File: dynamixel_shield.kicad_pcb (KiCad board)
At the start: 2 copper layers, 68.6 x 53.3 mm, 25 parts, among them P1 BARREL_JACK, P2 CONN_01X02, P3 CONN_01X03, P4 CONN_01X03, P5 CONN_01X03, P6 CONN_01X03, P7 CONN_01X03, P8 CONN_01X03, P9 CONN_01X03, Q1 MOSFET_N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

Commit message: Update silkscreen
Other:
- board text added: "10A MAX"
- board text added: "5A MAX"
- board text added: "POWER (12V)"
- board text added: "VIN POWER"
- board text removed: "VIN"
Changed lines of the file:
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@@
     (area 53.318999 50.945 132.842001 112.522001)
     (thickness 1.6)
-    (drawings 16)
+    (drawings 19)
     (tracks 185)
     (zones 0)
@@
     (visible_elements FFFFFF7F)
     (pcbplotparams
-      (layerselection 0x00030_80000001)
+      (layerselection 0x010f0_80000001)
       (usegerberextensions false)
       (excludeedgelayer true)
@@
       (outputformat 1)
       (mirror false)
-      (drillshape 1)
+      (drillshape 0)
       (scaleselection 1)
-      (outputdirectory ""))
+      (outputdirectory gerber/))
   )
   (net 0 "")
@@
     (descr "Bornier d'alimentation 2 pins")
     (tags DEV)
-    (fp_text reference P2 (at 0 -5.08 270) (layer F.SilkS)
+    (fp_text reference P2 (at -5.842 0 360) (layer F.SilkS)
       (effects (font (size 1 1) (thickness 0.15)))
     )
@@
     (descr "DC Barrel Jack")
     (tags "Power Jack")
-    (fp_text reference P1 (at 9.144 0 90) (layer F.SilkS)
+    (fp_text reference P1 (at -0.254 5.588 180) (layer F.SilkS)
       (effects (font (size 1 1) (thickness 0.15)))
     )
@@
     (descr "Fuseholder, 5x20, open, horizontal, Type-II, lateral,")
     (tags "Fuseholder, 5x20, open, horizontal, Type-II, lateral, Sicherungshalter, offen,")
-    (fp_text reference F1 (at 0 -5.08) (layer F.SilkS)
+    (fp_text reference F1 (at 0 -0.762) (layer F.SilkS)
       (effects (font (size 1 1) (thickness 0.15)))
     )
@@
       (net 38 "Net-(F1-Pad1)"))
   )
+  (gr_text "POWER (12V)" (at 67.056 93.472) (layer F.SilkS)
+    (effects (font (size 1 1) (thickness 0.15)))
+  )
+  (gr_text "5A\nMAX" (at 73.406 99.822 90) (layer F.SilkS)
+    (effects (font (size 1 1) (thickness 0.15)))
+  )
+  (gr_text "10A\nMAX" (at 72.39 87.122 90) (layer F.SilkS)
+    (effects (font (size 1 1) (thickness 0.15)))
+  )
   (gr_text https://github.com/descampsa/DynamixelShield (at 81.788 79.502) (layer B.SilkS)
     (effects (font (size 1 1) (thickness 0.15)) (justify mirror))
@@
     (effects (font (size 1 1) (thickness 0.15)))
   )
-  (gr_text VIN (at 110.744 93.98) (layer F.SilkS)
+  (gr_text "VIN POWER" (at 110.744 93.98) (layer F.SilkS)
     (effects (font (size 1 1) (thickness 0.15)))
   )

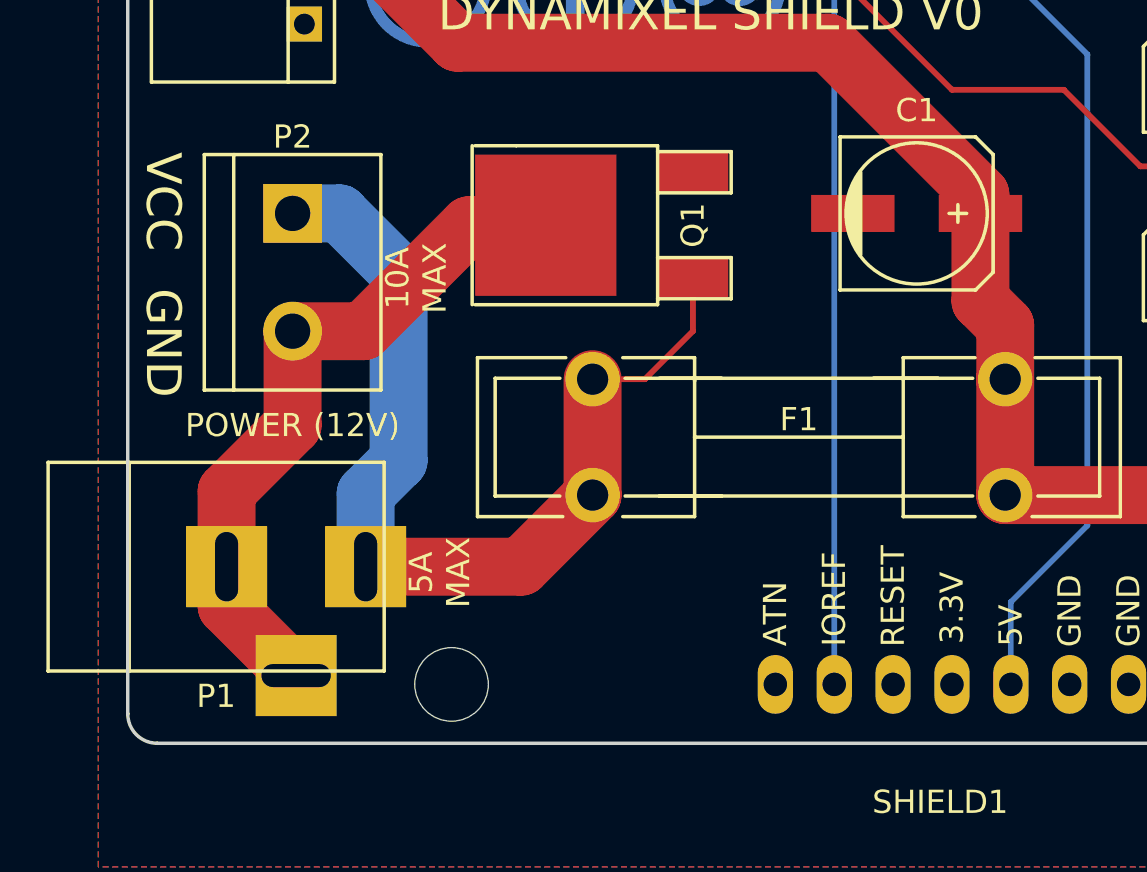
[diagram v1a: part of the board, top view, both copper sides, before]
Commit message: Add power on LED
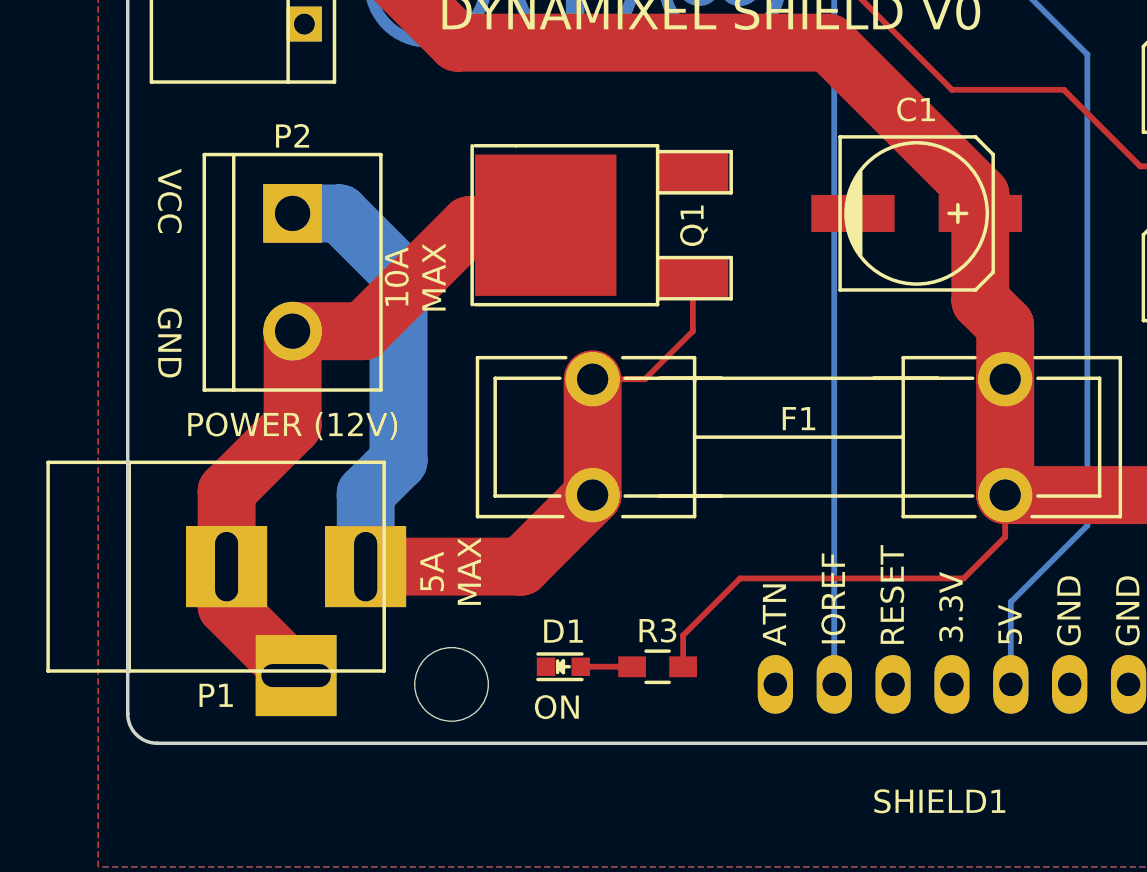
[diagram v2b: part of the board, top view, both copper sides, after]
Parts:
- added D1: LED, LEDs:LED_0603, F.Cu at (78.7, 103.9)
- added R3: 10K, Resistors_SMD:R_0603_HandSoldering, F.Cu at (82.8, 103.9)
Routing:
- net +12V: track 122.1 -> 140.9 mm
- net Net-(D1-Pad2): track 0.00 -> 2.21 mm
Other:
- board text added: "ON"
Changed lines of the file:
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@@
 (kicad_pcb (version 4) (host pcbnew 4.0.1-product)
   (general
-    (links 57)
+    (links 60)
     (no_connects 0)
     (area 53.318999 50.945 132.842001 112.522001)
     (thickness 1.6)
-    (drawings 19)
-    (tracks 185)
+    (drawings 20)
+    (tracks 191)
     (zones 0)
-    (modules 25)
-    (nets 40)
+    (modules 27)
+    (nets 41)
   )
   (page A4)
@@
   (net 38 "Net-(F1-Pad1)")
   (net 39 "Net-(P1-Pad2)")
+  (net 40 "Net-(D1-Pad2)")
   (net_class Default "This is the default net class."
     (clearance 0.2)
@@
     (add_net /TXD)
     (add_net GND)
+    (add_net "Net-(D1-Pad2)")
     (add_net "Net-(JP1-Pad4)")
     (add_net "Net-(JP4-Pad3)")
@@
       (net 38 "Net-(F1-Pad1)"))
   )
+  (module LEDs:LED_0603 (layer F.Cu)
+    (at 78.74 103.886)
+    (descr "LED 0603 smd package")
+    (tags "LED led 0603 SMD smd SMT smt smdled SMDLED smtled SMTLED")
+    (attr smd)
+    (fp_text reference D1 (at 0 -1.5) (layer F.SilkS)
+      (effects (font (size 1 1) (thickness 0.15)))
+    )
+    (fp_text value LED (at 0 1.5) (layer F.Fab)
+      (effects (font (size 1 1) (thickness 0.15)))
+    )
+    (fp_line (start -0.3 -0.2) (end -0.3 0.2) (layer F.Fab) (width 0.15))
+    (fp_line (start -0.2 0) (end 0.1 -0.2) (layer F.Fab) (width 0.15))
+    (fp_line (start 0.1 0.2) (end -0.2 0) (layer F.Fab) (width 0.15))
+    (fp_line (start 0.1 -0.2) (end 0.1 0.2) (layer F.Fab) (width 0.15))
+    (fp_line (start 0.8 0.4) (end -0.8 0.4) (layer F.Fab) (width 0.15))
+    (fp_line (start 0.8 -0.4) (end 0.8 0.4) (layer F.Fab) (width 0.15))
+    (fp_line (start -0.8 -0.4) (end 0.8 -0.4) (layer F.Fab) (width 0.15))
+    (fp_line (start -0.8 0.4) (end -0.8 -0.4) (layer F.Fab) (width 0.15))
+    (fp_line (start -1.1 0.55) (end 0.8 0.55) (layer F.SilkS) (width 0.15))
+    (fp_line (start -1.1 -0.55) (end 0.8 -0.55) (layer F.SilkS) (width 0.15))
+    (fp_line (start -0.2 0) (end 0.25 0) (layer F.SilkS) (width 0.15))
+    (fp_line (start -0.25 -0.25) (end -0.25 0.25) (layer F.SilkS) (width 0.15))
+    (fp_line (start -0.25 0) (end 0 -0.25) (layer F.SilkS) (width 0.15))
+    (fp_line (start 0 -0.25) (end 0 0.25) (layer F.SilkS) (width 0.15))
+    (fp_line (start 0 0.25) (end -0.25 0) (layer F.SilkS) (width 0.15))
+    (fp_line (start 1.4 -0.75) (end 1.4 0.75) (layer F.CrtYd) (width 0.05))
+    (fp_line (start 1.4 0.75) (end -1.4 0.75) (layer F.CrtYd) (width 0.05))
+    (fp_line (start -1.4 0.75) (end -1.4 -0.75) (layer F.CrtYd) (width 0.05))
+    (fp_line (start -1.4 -0.75) (end 1.4 -0.75) (layer F.CrtYd) (width 0.05))
+    (pad 2 smd rect (at 0.7493 0 180) (size 0.79756 0.79756) (layers F.Cu F.Paste F.Mask)
+      (net 40 "Net-(D1-Pad2)"))
+    (pad 1 smd rect (at -0.7493 0 180) (size 0.79756 0.79756) (layers F.Cu F.Paste F.Mask)
+      (net 11 GND))
+    (model LEDs.3dshapes/LED_0603.wrl
+      (at (xyz 0 0 0))
+      (scale (xyz 1 1 1))
+      (rotate (xyz 0 0 180))
+    )
+  )
+  (module Resistors_SMD:R_0603_HandSoldering (layer F.Cu)
+    (at 82.804 103.886 180)
+    (descr "Resistor SMD 0603, hand soldering")
+    (tags "resistor 0603")
+    (attr smd)
+    (fp_text reference R3 (at 0 1.524 180) (layer F.SilkS)
+      (effects (font (size 1 1) (thickness 0.15)))
+    )
+    (fp_text value 10K (at 0 -1.524 180) (layer F.Fab)
+      (effects (font (size 1 1) (thickness 0.15)))
+    )
+    (fp_line (start -2 -0.8) (end 2 -0.8) (layer F.CrtYd) (width 0.05))
+    (fp_line (start -2 0.8) (end 2 0.8) (layer F.CrtYd) (width 0.05))
+    (fp_line (start -2 -0.8) (end -2 0.8) (layer F.CrtYd) (width 0.05))
+    (fp_line (start 2 -0.8) (end 2 0.8) (layer F.CrtYd) (width 0.05))
+    (fp_line (start 0.5 0.675) (end -0.5 0.675) (layer F.SilkS) (width 0.15))
+    (fp_line (start -0.5 -0.675) (end 0.5 -0.675) (layer F.SilkS) (width 0.15))
+    (pad 1 smd rect (at -1.1 0 180) (size 1.2 0.9) (layers F.Cu F.Paste F.Mask)
+      (net 9 +12V))
+    (pad 2 smd rect (at 1.1 0 180) (size 1.2 0.9) (layers F.Cu F.Paste F.Mask)
+      (net 40 "Net-(D1-Pad2)"))
+    (model Resistors_SMD.3dshapes/R_0603_HandSoldering.wrl
+      (at (xyz 0 0 0))
+      (scale (xyz 1 1 1))
+      (rotate (xyz 0 0 0))
+    )
+  )
+  (gr_text ON (at 78.486 105.664) (layer F.SilkS)
+    (effects (font (size 1 1) (thickness 0.15)))
+  )
   (gr_text "POWER (12V)" (at 67.056 93.472) (layer F.SilkS)
     (effects (font (size 1 1) (thickness 0.15)))
   )
-  (gr_text "5A\nMAX" (at 73.406 99.822 90) (layer F.SilkS)
+  (gr_text "5A\nMAX" (at 73.914 99.822 90) (layer F.SilkS)
     (effects (font (size 1 1) (thickness 0.15)))
   )
@@
     (effects (font (size 1 1) (thickness 0.15)))
   )
-  (gr_text GND (at 61.468 89.916 270) (layer F.SilkS)
-    (effects (font (size 1.5 1.5) (thickness 0.3)))
-  )
-  (gr_text VCC (at 61.468 83.82 270) (layer F.SilkS)
-    (effects (font (size 1.5 1.5) (thickness 0.3)))
+  (gr_text GND (at 61.722 89.916 270) (layer F.SilkS)
+    (effects (font (size 1 1) (thickness 0.15)))
+  )
+  (gr_text VCC (at 61.722 83.82 270) (layer F.SilkS)
+    (effects (font (size 1 1) (thickness 0.15)))
   )
   (segment (start 118.364 56.388) (end 118.364 60.96) (width 0.25) (layer F.Cu) (net 1))
@@
   (segment (start 113.792 60.452) (end 94.996 60.452) (width 0.25) (layer B.Cu) (net 8))
   (segment (start 115.824 58.42) (end 113.792 60.452) (width 0.25) (layer B.Cu) (net 8))
+  (segment (start 83.904 103.886) (end 83.904 102.532) (width 0.25) (layer F.Cu) (net 9) (status 400000))
+  (segment (start 97.8 98.288) (end 97.8 96.48) (width 0.25) (layer F.Cu) (net 9) (status 800000))
+  (segment (start 96.012 100.076) (end 97.8 98.288) (width 0.25) (layer F.Cu) (net 9))
+  (segment (start 86.36 100.076) (end 96.012 100.076) (width 0.25) (layer F.Cu) (net 9))
+  (segment (start 83.904 102.532) (end 86.36 100.076) (width 0.25) (layer F.Cu) (net 9))
   (segment (start 97.8 91.48) (end 97.8 89.164) (width 2.5) (layer F.Cu) (net 9))
   (segment (start 96.73082 88.09482) (end 96.73082 84.328) (width 2.5) (layer F.Cu) (net 9))
@@
   (segment (start 67.056 93.472) (end 67.056 89.408) (width 2.5) (layer F.Cu) (net 39))
   (segment (start 64.20866 96.31934) (end 67.056 93.472) (width 2.5) (layer F.Cu) (net 39))
+  (segment (start 81.704 103.886) (end 79.4893 103.886) (width 0.25) (layer F.Cu) (net 40) (status C00000))
   (zone (net 11) (net_name GND) (layer F.Cu) (hatch edge 0.508)
     (connect_pads (clearance 0.254))

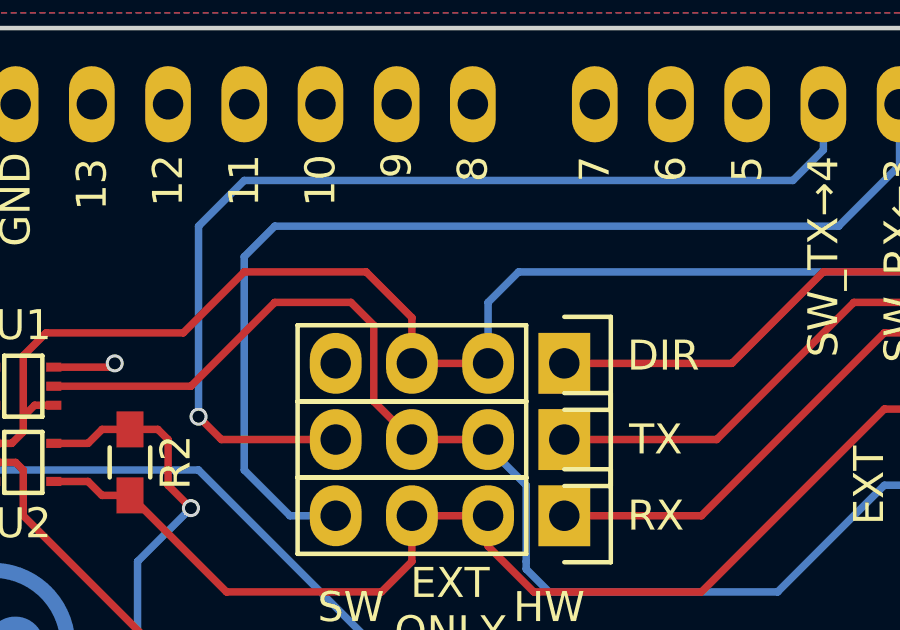
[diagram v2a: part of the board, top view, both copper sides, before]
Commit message: Fix error in schematics
Arduino direction port was not connected in the SW configuration.
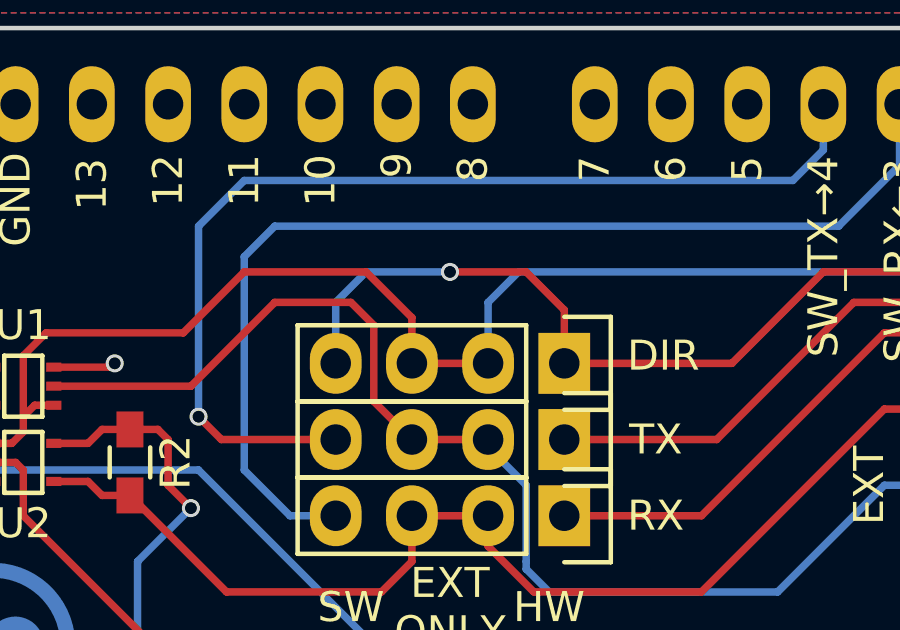
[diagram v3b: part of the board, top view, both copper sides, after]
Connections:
- JP1 pad 4: Net-(JP1-Pad4) -> /ARDUINO_DIRECTION_PORT
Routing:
- net /ARDUINO_DIRECTION_PORT: track 20.0 -> 32.3 mm, vias 0 -> 1

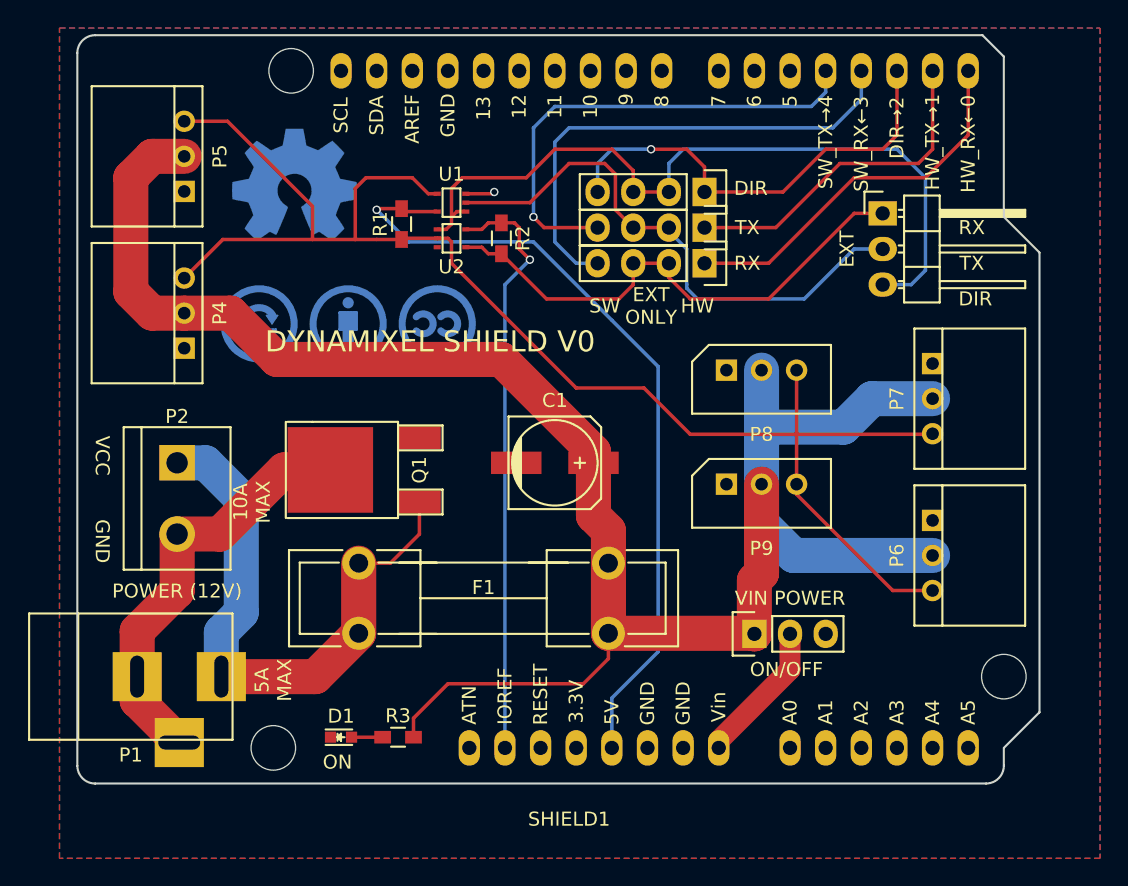
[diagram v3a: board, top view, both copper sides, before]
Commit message: move ext connector to make place for the fourth mounting hole
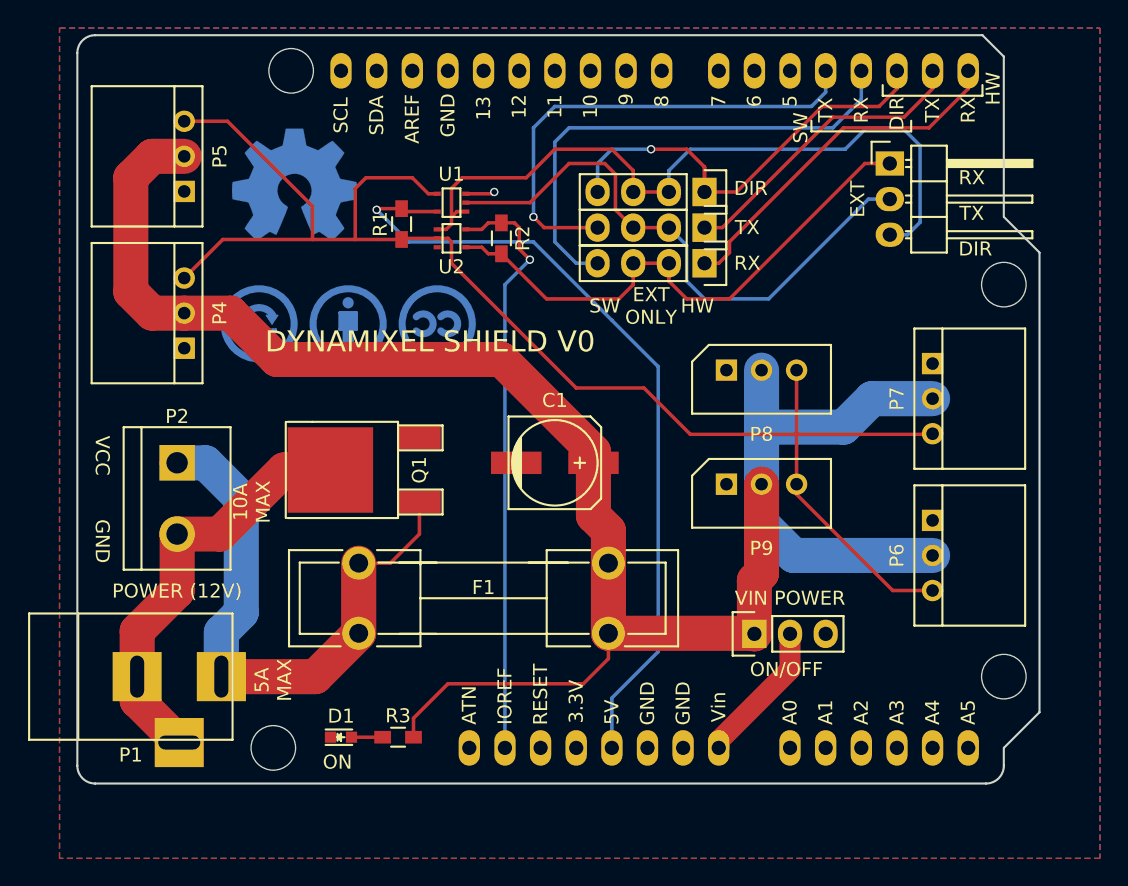
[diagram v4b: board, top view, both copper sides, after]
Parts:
- moved P3 3.59 mm to (117.9, 63.0)
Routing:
- net /RXD: track 37.4 -> 40.5 mm
- net /HW_TXD: track 24.2 -> 21.6 mm
- net /DIRECTION_PORT: track 55.9 -> 53.4 mm
- net /TXD: track 39.6 -> 41.6 mm
- net /HW_RXD: track 27.2 -> 25.7 mm
